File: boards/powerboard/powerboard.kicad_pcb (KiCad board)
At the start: 2 copper layers, 184 parts, among them J101 RXSM experiment connector, J102 Powerboard <-> Mainboard, J103 Cameraboard, J104 BLDC Motor, J105 BOOST, J106 Boost24V_EN, J107 24V_1, J108 24V_2, J109 24V_3, J110 BAT, J111 GND, J801 Heat probe power, P501 10k NTC, Q101 SQM40031EL, Q102 DMN6140L, Q104 DMN6140L, Q501 DMN6140L, Q502 PMV27UPE, Q503 IRF7343PBF, Q801 BUK7Y4R8-60E, Q802 BUK7Y4R8-60E, Q803 BUK7Y4R8-60E, U1001 LT3592, U101 LM1117-3.3, U102 DS26LV32AT, U1101 LMV324, U1102 LMV324, U201 LMZ14203, U301 LM3480-12, U302 DRV8332, U303 ACS711, U501 LTC4010, U601 PC3H7, U602 PC3H7, U603 PC3H7, U701 MAX13432EESD, U801 ACS711, U802 ACS711, U803 ACS711, U901 AD7928, U902 REF3025

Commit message: [powerboard] layout: parts placed; RS-422 termination added; various minor improvements
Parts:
- added C109: 100n, Capacitors_SMD:C_0603, B.Cu at (160.7, 80.0)
- added J112: M3, Mounting_Holes:MountingHole_3.2mm_M3_Pad, F.Cu at (132.7, 125.7)
- added J113: M3, Mounting_Holes:MountingHole_3.2mm_M3_Pad, F.Cu at (132.7, 62.9)
- added J114: M3, Mounting_Holes:MountingHole_3.2mm_M3_Pad, F.Cu at (210.2, 125.7)
- added J115: M3, Mounting_Holes:MountingHole_3.2mm_M3_Pad, F.Cu at (210.2, 62.9)
- added J116: M3, Mounting_Holes:MountingHole_3.2mm_M3_Pad, F.Cu at (114.3, 94.0)
- added J117: M3, Mounting_Holes:MountingHole_3.2mm_M3_Pad, F.Cu at (172.1, 94.0)
- added R113: 15k, Resistors_SMD:R_0603, F.Cu at (220.6, 82.8)
- added R114: 1k, Resistors_SMD:R_0603, F.Cu at (220.6, 86.6)
- added R115: NC, Resistors_SMD:R_0603, B.Cu at (142.2, 126.4)
- added R116: NC, Resistors_SMD:R_0603, F.Cu at (127.6, 64.2)
- added R117: NC, Resistors_SMD:R_0603, F.Cu at (207.0, 121.9)
- added R118: NC, Resistors_SMD:R_0603, B.Cu at (200.0, 62.9)
- added R119: NC, Resistors_SMD:R_0603, F.Cu at (114.3, 88.9)
- added R120: NC, Resistors_SMD:R_0603, F.Cu at (174.1, 99.1)
- added R607: 1k, Resistors_SMD:R_0603, F.Cu at (160.1, 121.9)
- added R608: 1k, Resistors_SMD:R_0603, F.Cu at (156.1, 121.9)
- C1003, C201, C206, C501, C801, C802, C803, C901, FL101, FL102, J102, L501, Q503, Q801, Q802, Q803, R501, R507, R601, R602, R603, R804, R805, R806, U102, U801, U802, U803, U901: moved to B.Cu
- J101: footprint Connectors:DB9MD -> Connectors:DB15MD
- J801: footprint Mounting_Holes:MountingHole_3.2mm_M3_Pad_Via -> Connectors:DB25FD
- U101: footprint TO_SOT_Packages_SMD:SOT-223-3Lead_TabPin2 -> TO_SOT_Packages_SMD:SOT-223
- moved C1101 167.0 mm to (219.5, 218.9)
- moved C1102 167.0 mm to (229.9, 218.9)
- moved C1103 167.0 mm to (219.5, 229.0)
- moved C1104 167.0 mm to (250.7, 228.9)
- moved C1106 167.0 mm to (224.7, 229.0)
- moved C1109 167.0 mm to (235.1, 218.9)
- moved C1111 167.0 mm to (229.9, 229.0)
- moved C1113 167.0 mm to (240.3, 218.9)
- moved C1116 167.0 mm to (224.7, 218.9)
- moved R1101 167.0 mm to (240.3, 228.9)
- moved R1115 167.0 mm to (242.3, 233.9)
- moved R1116 167.0 mm to (240.3, 223.9)
- moved C1105 167.0 mm to (224.7, 223.9)
- moved C1107 167.0 mm to (219.5, 223.9)
- moved C1108 167.0 mm to (229.9, 223.9)
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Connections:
- D701 pad 1: /RXSM_RX_~Z -> /RXSM_RX_Y
- D701 pad 2: /RXSM_RX_Y -> /RXSM_RX_~Z
- D702 pad 1: /RXSM_RX_~B -> /RXSM_RX_A
- D702 pad 2: /RXSM_RX_A -> /RXSM_RX_~B
- FL101 pad 2: /RXSM_Ground -> /RXSM_28V
- FL101 pad 4: /RXSM_28V -> /RXSM_Ground
- FL102 pad 2: (no net) -> /Powerboard Battery Charging/charge_power
- FL102 pad 4: /Powerboard Battery Charging/charge_power -> /RXSM_charge-
- FL701 pad 2: Net-(FL701-Pad2) -> /RXSM_RX_A
- FL701 pad 4: /RXSM_RX_A -> Net-(FL701-Pad4)
- FL702 pad 2: Net-(FL702-Pad2) -> /RXSM_RX_Y
- FL702 pad 4: /RXSM_RX_Y -> Net-(FL702-Pad4)
- J102 pad 16: (no net) -> /extADC_SPI_SCK
- J102 pad 17: (no net) -> /extADC_SPI_MISO
- J102 pad 18: (no net) -> /extADC_SPI_MOSI
- J102 pad 19: (no net) -> /extADC_SPI_CS1
- J107 pad 1: /Powerboard_Heat_Probes/24V_BAT_1 -> /24V_BAT_1
- J108 pad 1: (no net) -> /24V_BAT_2
- J109 pad 1: (no net) -> /24V_BAT_3
- J801 pad 1: /Powerboard_Heat_Probes/24V_BAT_1 -> /24V_BAT_1
- R106 pad 1: (no net) -> /24V_BAT_3
- R108 pad 1: (no net) -> /24V_BAT_2
- R1109 pad 2: GND -> /Powerboard_ADC_Filter/IN4
- U102 pad 10: /Encoder_A+ -> (no net)
- U102 pad 11: /Encoder_A -> (no net)
- U102 pad 5: (no net) -> /Encoder_A
- U102 pad 6: (no net) -> /Encoder_A+
- U102 pad 7: (no net) -> /Encoder_A-
- U102 pad 9: /Encoder_A- -> (no net)
- U701 pad 10: Net-(FL702-Pad2) -> Net-(FL702-Pad4)
- U701 pad 11: Net-(FL701-Pad2) -> Net-(FL701-Pad4)
- U901 pad 1: (no net) -> /extADC_SPI_SCK
- U901 pad 18: (no net) -> /extADC_SPI_MISO
- U901 pad 2: (no net) -> /extADC_SPI_MOSI
- U901 pad 3: (no net) -> /extADC_SPI_CS1
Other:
- board outline added: 102.2 x 69.2 mm
- rule pad_to_mask_clearance: 0.2 -> 0.05

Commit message: [powerboard] all parts placed, pcb outline
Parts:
- added J118: M3, Mounting_Holes:MountingHole_3.2mm_M3_Pad, F.Cu at (119.4, 125.7)
- added R121: NC, Resistors_SMD:R_0603, F.Cu at (125.1, 125.7)
- C1101, C1102, C1103, C1104, C1105, C1106, C1107, C1108, C318, D303, D305, R1101, R1102, R1103, R1104, R1105, R1106, R1107, R1108, R111, U1101, U303: moved to B.Cu
- R115: moved to F.Cu
- moved L301 255.2 mm to (187.7, 70.7), turned to 90 degrees
- moved C318 252.7 mm to (193.8, 60.7), turned to 180 degrees
- moved C309 249.4 mm to (177.0, 77.7), turned to 270 degrees
- moved C312 249.3 mm to (160.8, 71.9)
- moved D304 249.0 mm to (193.1, 76.7)
- moved C310 248.9 mm to (177.0, 82.8), turned to 270 degrees
- moved C316 246.8 mm to (194.1, 67.3)
- moved C314 244.2 mm to (178.6, 78.5), turned to 270 degrees
- moved C311 244.0 mm to (173.5, 88.1), turned to 180 degrees
- moved C315 242.3 mm to (178.6, 73.7), turned to 90 degrees
- moved D303 241.5 mm to (166.1, 87.1), turned to 90 degrees
- moved D305 241.4 mm to (189.2, 73.4)
- moved R302 239.3 mm to (158.2, 74.4), turned to 180 degrees
- moved D301 239.0 mm to (156.5, 72.6), turned to 270 degrees
- moved C304 238.0 mm to (160.8, 85.6)
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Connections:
- J104 pad 1: /Phase_U -> /Hall_U
- J104 pad 11: /Hall_V -> /Encoder_A-
- J104 pad 12: +5V -> /Encoder_B-
- J104 pad 13: /Encoder_A+ -> +5V
- J104 pad 14: /Encoder_B+ -> /Phase_U
- J104 pad 15: +5V -> /Phase_W
- J104 pad 2: /Phase_W -> /Hall_W
- J104 pad 3: /Hall_U -> /Encoder_A+
- J104 pad 4: /Hall_W -> /Encoder_B+
- J104 pad 5: GND -> Net-(J104-Pad5)
- J104 pad 6: /Encoder_A- -> +5V
- J104 pad 7: /Encoder_B- -> /Phase_V
- J104 pad 8: Net-(J104-Pad8) -> GND
- J104 pad 9: /Phase_V -> /Hall_V
- R111 pad 1: Net-(J104-Pad8) -> Net-(J104-Pad5)
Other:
- board size 102.2 x 69.2 mm -> 97.2 x 69.2 mm

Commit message: [powerboard] first layout (wip)
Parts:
- moved R111 22.8 mm to (143.0, 81.2), turned to 270 degrees
- moved C109 4.58 mm to (159.1, 84.3)
- moved U102 4.58 mm to (157.9, 78.6)
- moved R110 4.00 mm to (139.1, 81.3)
- moved C901 3.94 mm to (143.4, 98.4)
- moved U901 3.78 mm to (141.2, 94.2)
- moved C206 3.28 mm to (139.4, 115.8)
- moved C701 0.77 mm to (122.7, 97.3), turned to 270 degrees
- moved J105 0.64 mm to (197.5, 124.5)
- moved J106 0.64 mm to (172.1, 120.0)
- moved J110 0.64 mm to (179.7, 124.5)
- moved J111 0.64 mm to (188.6, 124.5)
- moved J114 0.64 mm to (210.2, 125.1)
- moved J118 0.64 mm to (119.4, 125.1)
- moved P501 0.64 mm to (168.3, 120.0)
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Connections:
- net Net-(L501-Pad1) renamed /Powerboard Battery Charging/bat_inductor
- J801 pad 11: Net-(J801-Pad11) -> /Powerboard_Heat_Probes/Probe3
- J801 pad 12: Net-(J801-Pad11) -> /Powerboard_Heat_Probes/Probe3
- J801 pad 16: Net-(J801-Pad16) -> /Powerboard_Heat_Probes/Probe1
- J801 pad 17: Net-(J801-Pad16) -> /Powerboard_Heat_Probes/Probe1
- J801 pad 20: Net-(J801-Pad20) -> /Powerboard_Heat_Probes/Probe2
- J801 pad 21: Net-(J801-Pad20) -> /Powerboard_Heat_Probes/Probe2
- J801 pad 24: Net-(J801-Pad11) -> /Powerboard_Heat_Probes/Probe3
- J801 pad 25: Net-(J801-Pad11) -> /Powerboard_Heat_Probes/Probe3
- J801 pad 3: Net-(J801-Pad16) -> /Powerboard_Heat_Probes/Probe1
- J801 pad 4: Net-(J801-Pad16) -> /Powerboard_Heat_Probes/Probe1
- J801 pad 7: Net-(J801-Pad20) -> /Powerboard_Heat_Probes/Probe2
- J801 pad 8: Net-(J801-Pad20) -> /Powerboard_Heat_Probes/Probe2
- Q801 pad 1: /Powerboard_Heat_Probes/Probe1 -> /Powerboard_Heat_Probes/Probe1_sense
- Q801 pad 2: /Powerboard_Heat_Probes/Probe1 -> /Powerboard_Heat_Probes/Probe1_sense
- Q801 pad 3: /Powerboard_Heat_Probes/Probe1 -> /Powerboard_Heat_Probes/Probe1_sense
- Q801 pad 5: Net-(J801-Pad16) -> /Powerboard_Heat_Probes/Probe1
- Q802 pad 1: /Powerboard_Heat_Probes/Probe2 -> /Powerboard_Heat_Probes/Probe2_sense
- Q802 pad 2: /Powerboard_Heat_Probes/Probe2 -> /Powerboard_Heat_Probes/Probe2_sense
- Q802 pad 3: /Powerboard_Heat_Probes/Probe2 -> /Powerboard_Heat_Probes/Probe2_sense
- Q802 pad 5: Net-(J801-Pad20) -> /Powerboard_Heat_Probes/Probe2
- Q803 pad 1: /Powerboard_Heat_Probes/Probe3 -> /Powerboard_Heat_Probes/Probe3_sense
- Q803 pad 2: /Powerboard_Heat_Probes/Probe3 -> /Powerboard_Heat_Probes/Probe3_sense
- Q803 pad 3: /Powerboard_Heat_Probes/Probe3 -> /Powerboard_Heat_Probes/Probe3_sense
- Q803 pad 5: Net-(J801-Pad11) -> /Powerboard_Heat_Probes/Probe3
- R804 pad 1: /Powerboard_Heat_Probes/Probe1 -> /Powerboard_Heat_Probes/Probe1_sense
- R805 pad 1: /Powerboard_Heat_Probes/Probe2 -> /Powerboard_Heat_Probes/Probe2_sense
- R806 pad 1: /Powerboard_Heat_Probes/Probe3 -> /Powerboard_Heat_Probes/Probe3_sense
- U801 pad 1: /Powerboard_Heat_Probes/Probe1 -> /Powerboard_Heat_Probes/Probe1_sense
- U801 pad 2: /Powerboard_Heat_Probes/Probe1 -> /Powerboard_Heat_Probes/Probe1_sense
- U802 pad 1: /Powerboard_Heat_Probes/Probe2 -> /Powerboard_Heat_Probes/Probe2_sense
- U802 pad 2: /Powerboard_Heat_Probes/Probe2 -> /Powerboard_Heat_Probes/Probe2_sense
- U803 pad 1: /Powerboard_Heat_Probes/Probe3 -> /Powerboard_Heat_Probes/Probe3_sense
- U803 pad 2: /Powerboard_Heat_Probes/Probe3 -> /Powerboard_Heat_Probes/Probe3_sense
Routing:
- net GND: track 0.00 -> 273.1 mm, vias 0 -> 13
- net /RXSM_28V: track 0.00 -> 208.5 mm, vias 0 -> 7
- net +3V3: track 0.00 -> 171.3 mm, vias 0 -> 7
- net +5V: track 0.00 -> 97.8 mm, vias 0 -> 4
- net /RXSM_LO: track 0.00 -> 60.6 mm, vias 0 -> 2
- net /RXSM_SOE: track 0.00 -> 60.4 mm, vias 0 -> 2
- net /RXSM_RX_~B: track 0.00 -> 53.9 mm, vias 0 -> 1
- net /RXSM_RX_~Z: track 0.00 -> 53.2 mm
- net /RXSM_SODS: track 0.00 -> 52.7 mm, vias 0 -> 2
- net /Charge_status: track 0.00 -> 46.3 mm, vias 0 -> 2
- net /RXSM_RX_Y: track 0.00 -> 44.6 mm
- net /RXSM_RX_A: track 0.00 -> 43.8 mm, vias 0 -> 1
- net /Charge_EN: track 0.00 -> 41.8 mm, vias 0 -> 3
- net Net-(U302-Pad23): track 0.00 -> 40.5 mm, vias 0 -> 5
- net /RX: track 0.00 -> 39.8 mm, vias 0 -> 1
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- added copper zone on B.Cu, net /24V_BAT_1
- added copper zone on F.Cu, net /24V_BAT_1
- added copper zone on B.Cu, net /24V_BAT_2
- added copper zone on F.Cu, net /24V_BAT_2
- added copper zone on B.Cu, net /24V_BAT_3
- added copper zone on F.Cu, net /24V_BAT_3
- added copper zone on B.Cu, net /BAT_10V
- added copper zone on F.Cu, net /BAT_10V
- added copper zone on B.Cu, net /BAT_raw
- added copper zone on F.Cu, net /BAT_raw
- added copper zone on B.Cu, net /Powerboard Battery Charging/bat_inductor
- added copper zone on B.Cu, net /Powerboard Battery Charging/bat_sense
- added copper zone on B.Cu, net /Powerboard_Heat_Probes/Probe1
- added copper zone on B.Cu, net /Powerboard_Heat_Probes/Probe1_sense
- added copper zone on B.Cu, net /Powerboard_Heat_Probes/Probe2
- added copper zone on B.Cu, net /Powerboard_Heat_Probes/Probe2_sense
- added copper zone on B.Cu, net /Powerboard_Heat_Probes/Probe3
- added copper zone on B.Cu, net /Powerboard_Heat_Probes/Probe3_sense
- added copper zone on B.Cu, net GND
- added copper zone on F.Cu, net GND
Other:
- board size 97.2 x 69.2 mm -> 97.2 x 68.6 mm
- rule trace_min: 0.2 -> 0.1

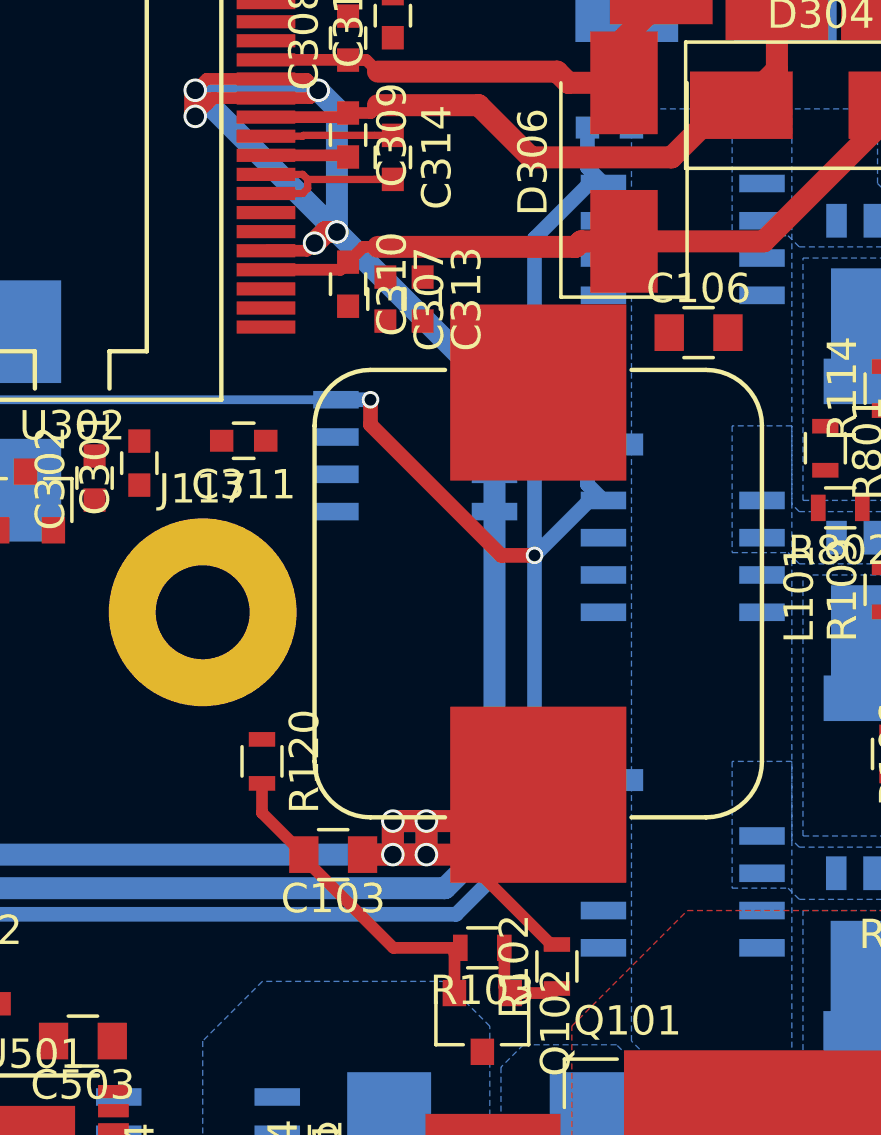
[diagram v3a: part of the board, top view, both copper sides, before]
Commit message: [powerboard] curreent measurement: compatibility with ACS725
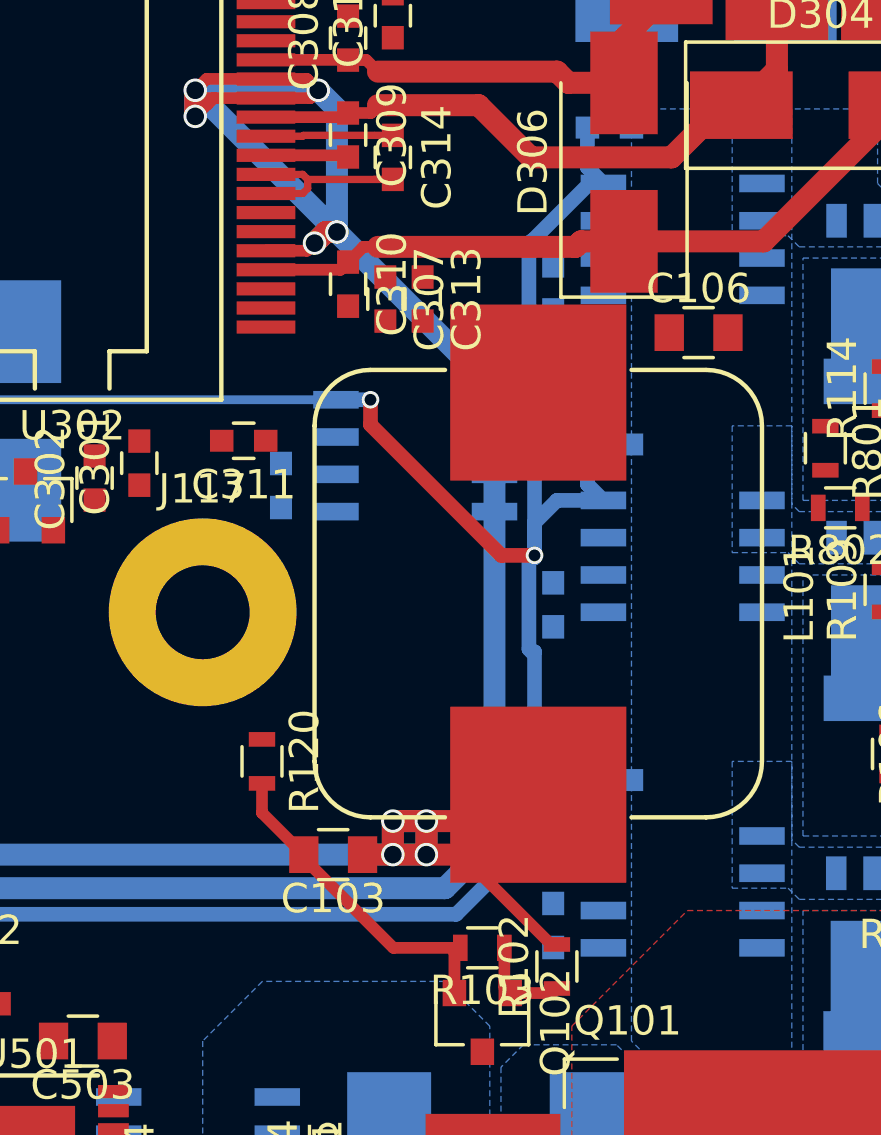
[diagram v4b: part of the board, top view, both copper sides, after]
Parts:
- added C319: 1n, Capacitors_SMD:C_0603, B.Cu at (174.8, 89.7)
- added C804: 1n, Capacitors_SMD:C_0603, B.Cu at (184.0, 82.9)
- added C805: 1n, Capacitors_SMD:C_0603, B.Cu at (184.0, 93.7)
- added C806: 1n, Capacitors_SMD:C_0603, B.Cu at (184.0, 104.6)
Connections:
- U303 pad 6: (no net) -> Net-(C319-Pad1)
- U801 pad 6: (no net) -> Net-(C804-Pad1)
- U802 pad 6: (no net) -> Net-(C805-Pad1)
- U803 pad 6: (no net) -> Net-(C806-Pad1)
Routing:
- net +3V3: track 171.3 -> 172.4 mm

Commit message: [powerboard] more layout...
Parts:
- R120: moved to B.Cu
- moved J106 47.6 mm to (140.3, 84.6)
- moved R120 6.50 mm to (176.7, 93.1), turned to 90 degrees
- moved R801 2.82 mm to (192.9, 85.6)
- moved R117 1.82 mm to (207.8, 120.3), turned to 90 degrees
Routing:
- net GND: track 273.1 -> 498.5 mm, vias 13 -> 25
- net /Probe2_EN: track 0.00 -> 69.7 mm, vias 0 -> 1
- net /Probe1_EN: track 0.00 -> 69.4 mm, vias 0 -> 1
- net /Probe3_EN: track 0.00 -> 67.6 mm, vias 0 -> 1
- net /Powerboard_ADC_Filter/IN6: track 0.00 -> 62.3 mm, vias 0 -> 2
- net /Powerboard_ADC_Filter/IN7: track 0.00 -> 61.3 mm, vias 0 -> 2
- net /Powerboard Motor Controller/12V: track 0.00 -> 61.2 mm, vias 0 -> 2
- net /Powerboard_ADC_Filter/IN4: track 0.00 -> 53.0 mm, vias 0 -> 2
- net /Probe1_Current: track 0.00 -> 48.9 mm, vias 0 -> 2
- net /Powerboard Motor Controller/V_IN: track 4.33 -> 49.0 mm, vias 0 -> 3
- net /BAT_raw: track 0.00 -> 44.0 mm
- net /Probe2_Current: track 0.00 -> 39.5 mm, vias 0 -> 2
- net /Powerboard_ADC_Filter/IN5: track 0.00 -> 37.5 mm, vias 0 -> 2
- net /Probe3_Current: track 0.00 -> 33.9 mm, vias 0 -> 2
- net /Motor1_Current: track 0.00 -> 23.7 mm
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
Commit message: [powerboard] layout finished; separate GND and GNDPWR signals
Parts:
- added J119: GND, Mounting_Holes:MountingHole_3.2mm_M3_Pad_Via, F.Cu at (209.6, 114.3)
- added R122: 0, Resistors_SMD:R_0603, B.Cu at (172.8, 116.3)
- added R123: 0, Resistors_SMD:R_0603, F.Cu at (159.3, 116.0)
- added R124: 0, Resistors_SMD:R_0603, B.Cu at (183.5, 107.7)
- moved R111 20.1 mm to (162.8, 84.3)
- moved C802 8.64 mm to (182.4, 96.1), turned to 180 degrees
- moved C801 8.20 mm to (184.2, 85.5)
- moved C902 6.99 mm to (144.1, 100.3)
- moved C803 6.33 mm to (182.0, 104.6), turned to 270 degrees
- moved C1003 4.63 mm to (156.1, 66.5), turned to 0 degrees
- moved U902 4.06 mm to (140.6, 99.4), turned to 180 degrees
- moved R1102 2.48 mm to (150.8, 91.3)
- moved R117 2.26 mm to (206.4, 122.0)
- moved J106 2.17 mm to (141.1, 82.5)
- moved C101 1.63 mm to (156.2, 115.2), turned to 0 degrees
- moved R1111 1.16 mm to (142.9, 88.3)
- moved C1115 0.65 mm to (139.3, 88.6)
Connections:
- C101 pad 2: GND -> GNDPWR
- C504 pad 2: GND -> GNDPWR
- C505 pad 2: GND -> GNDPWR
- FL102 pad 3: GND -> GNDPWR
- J101 pad 10: (no net) -> Net-(J101-Pad10)
- J101 pad 11: (no net) -> Net-(J101-Pad11)
- J103 pad 1: (no net) -> Net-(J103-Pad1)
- J103 pad 2: (no net) -> Net-(J103-Pad2)
- J111 pad 1: GND -> GNDPWR
- J801 pad 13: (no net) -> Net-(J801-Pad13)
- Q503 pad 1: GND -> GNDPWR
- U102 pad 10: (no net) -> Net-(U102-Pad10)
- U102 pad 11: (no net) -> Net-(U102-Pad11)
- U102 pad 13: (no net) -> Net-(U102-Pad13)
- U102 pad 14: (no net) -> Net-(U102-Pad14)
- U102 pad 15: (no net) -> Net-(U102-Pad15)
- U102 pad 9: (no net) -> Net-(U102-Pad9)
- U501 pad 1: (no net) -> Net-(U501-Pad1)
- U501 pad 13: GND -> GNDPWR
- U501 pad 16: (no net) -> Net-(U501-Pad16)
- U701 pad 13: (no net) -> Net-(U701-Pad13)
- U701 pad 7: (no net) -> Net-(U701-Pad7)
- U801 pad 3: GND -> GNDPWR
- U801 pad 4: GND -> GNDPWR
- U802 pad 3: GND -> GNDPWR
- U802 pad 4: GND -> GNDPWR
- U803 pad 3: GND -> GNDPWR
- U803 pad 4: GND -> GNDPWR
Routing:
- net GND: track 498.5 -> 873.9 mm, vias 25 -> 53
- net /Motor_U_N: track 0.00 -> 65.4 mm, vias 0 -> 1
- net /Motor_U_P: track 0.00 -> 64.8 mm, vias 0 -> 1
- net +5V: track 93.6 -> 157.7 mm, vias 3 -> 5
- net GNDPWR: track 0.00 -> 61.1 mm, vias 0 -> 2
- net /Motor_V_P: track 0.00 -> 59.7 mm, vias 0 -> 1
- net /EndSwitch: track 0.00 -> 56.2 mm, vias 0 -> 2
- net /Hall_W: track 0.00 -> 53.2 mm, vias 0 -> 1
- net /Hall_V: track 0.00 -> 52.6 mm
- net /Motor_V_N: track 0.00 -> 52.5 mm, vias 0 -> 2
- net /Motor_W_P: track 0.00 -> 50.8 mm
- net /Hall_U: track 0.00 -> 50.5 mm
- net /Motor_W_N: track 0.00 -> 49.8 mm, vias 0 -> 2
- net /Encoder_A: track 0.00 -> 36.9 mm
- net /Encoder_B: track 0.00 -> 34.0 mm
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- added copper zone on B.Cu, net GNDPWR
- added copper zone on F.Cu, net GNDPWR
